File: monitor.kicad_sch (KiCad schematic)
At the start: 54 parts, among them J1 USB_C_Plug, J2 USB_C_Receptacle_USB2.0_14P, J3 Display, J4 Program, J5 Boot, U1 STM32U031K8Ux, U2 TPSM365R6V3RDNR, U3 TMP117xxDRV, U4 REF5025ADGK, U5 CC6903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

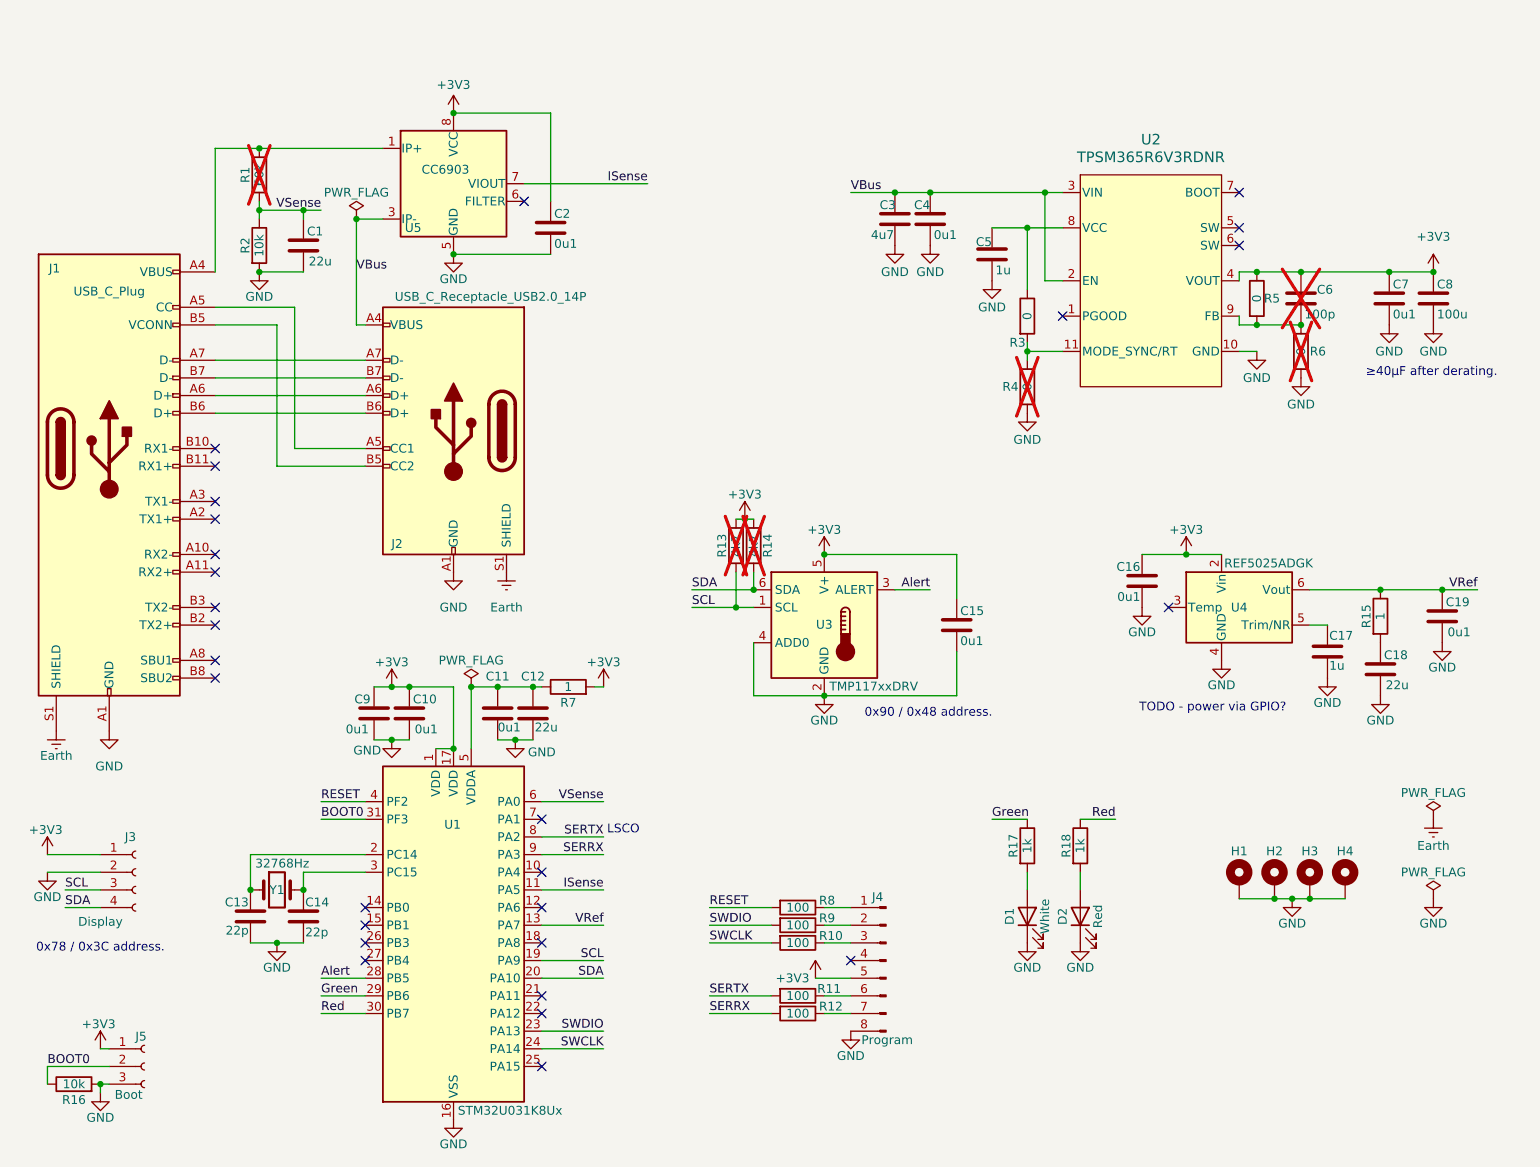
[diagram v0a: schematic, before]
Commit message: Monitor board layout
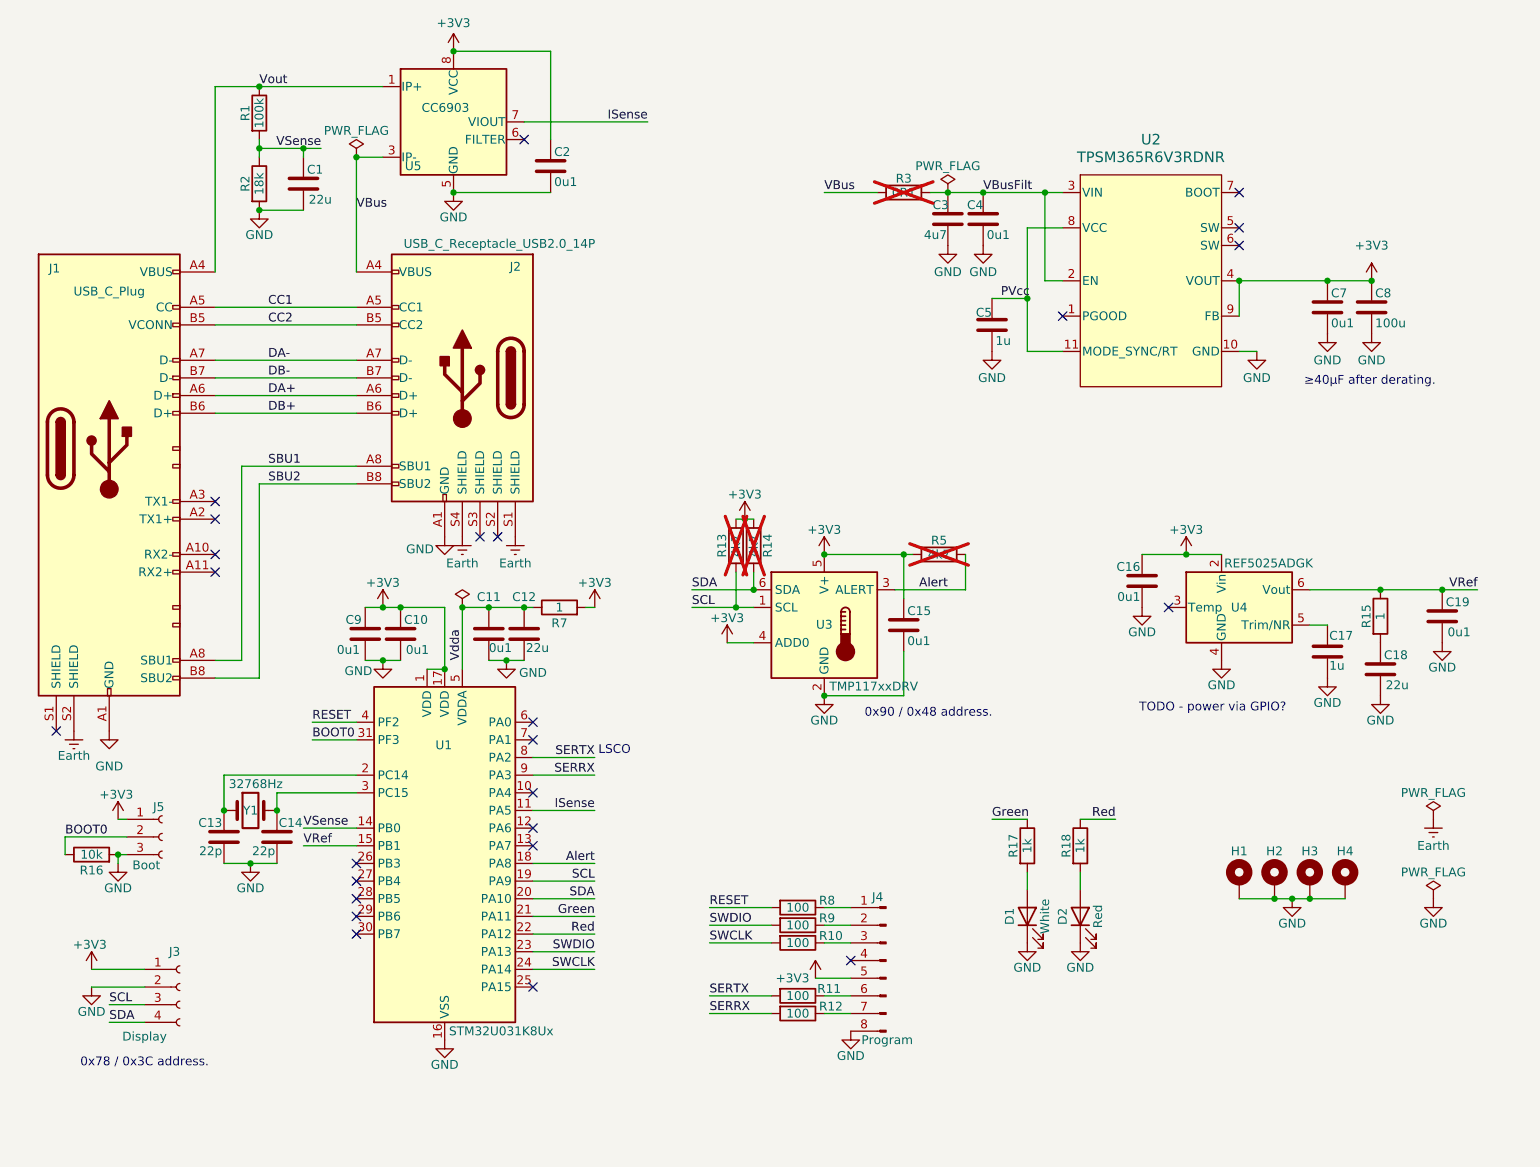
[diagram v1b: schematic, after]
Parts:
- removed C6: 100p, Capacitor_SMD:C_0603_1608Metric, symbol Device:C
- removed R4, R6: 0, Resistor_SMD:R_0603_1608Metric, symbol Device:R
- H1, H2, H3, H4: footprint MountingHole:MountingHole_3mm_Pad -> Parts:MountingHole_3mm_Pad
- J1: symbol Parts:USB_C_Plug -> Parts:USB_C_Plug_20; now in the parts list
- J2: footprint Connector_USB:USB_C_Receptacle_HRO_TYPE-C-31-M-12 -> Parts:USB_C_Receptacle_16P; symbol Parts:USB_C_Receptacle_USB2.0_14P -> Parts:USB_C_Receptacle_USB2.0_16P; now in the parts list
- J3: footprint Connector_PinSocket_2.54mm:PinSocket_1x03_P2.54mm_Vertical -> Parts:PinHeader_1x04_P2.54mm_Vertical
- J4: footprint Connector_PinHeader_2.54mm:PinHeader_1x08_P2.54mm_Vertical -> Parts:PinHeader_1x08_P2.54mm_Vertical
- J5: footprint Connector_PinSocket_2.54mm:PinSocket_1x03_P2.54mm_Vertical -> Parts:PinHeader_1x03_P2.54mm_Vertical
- R1: value 60k -> 100k; JLCPCB (none) -> C25803; now fitted
- R2: value 10k -> 18k; footprint Resistor_SMD:R_0402_1005Metric -> Resistor_SMD:R_0603_1608Metric; JLCPCB C25744 -> C25810
- R3: value 0 -> 0R1; JLCPCB C21189 -> (none); now not fitted; now left out of the parts list
- R5: value 0 -> 4k7; JLCPCB C21189 -> (none); now not fitted; now left out of the parts list
- U3: footprint Package_SON:WSON-6-1EP_2x2mm_P0.65mm_EP1x1.6mm -> Parts:WSON-6-1EP_2x2mm_P0.65mm_NoEP; symbol Sensor_Temperature:TMP117xxDRV -> Parts:TMP117xxDRV
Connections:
- net +3V3: now also U2.9 (FB), U3.4 (ADD0)
- net Alert: now also R5.2, U1.18 (PA8); no longer U1.28 (PB5)
- net Earth: now also J1.S2 (SHIELD), J2.S4 (SHIELD); no longer J1.S1 (SHIELD)
- net GND: no longer U3.4 (ADD0)
- net Green: now also U1.21 (PA11); no longer U1.29 (PB6)
- net Red: now also U1.22 (PA12); no longer U1.30 (PB7)
- net VBus: now also R3.1; no longer C3.1, C4.1, U2.2 (EN), U2.3 (VIN)
- net VRef: now also U1.15 (PB1); no longer U1.13 (PA7)
- net VSense: now also U1.14 (PB0); no longer U1.6 (PA0)
- net CC1: now reaches J1.A5 (CC), J2.A5 (CC1)
- net DA+: now reaches J1.A6 (D+), J2.A6 (D+)
- net DA-: now reaches J1.A7 (D-), J2.A7 (D-)
- net CC2: now reaches J1.B5 (VCONN), J2.B5 (CC2)
- net DB+: now reaches J1.B6 (D+), J2.B6 (D+)
- net DB-: now reaches J1.B7 (D-), J2.B7 (D-)
- net Vdda: now reaches C11.1, C12.1, R7.1, U1.5 (VDDA)
- net PVcc: now reaches U2.11 (MODE_SYNC/RT)
- net PVcc: now also C5.1, U2.8 (VCC); no longer R3.2
- net Vout: now reaches J1.A4 (VBUS), J1.A9 (VBUS), J1.B4 (VBUS), J1.B9 (VBUS), R1.1, U5.1 (IP+), U5.2 (IP+)
- net SBU1: now reaches J1.A8 (SBU1)
- net SBU1: now also J2.A8 (SBU1)
- net SBU2: now reaches J1.B8 (SBU2)
- net SBU2: now also J2.B8 (SBU2)
- new net VBusFilt: C3.1, C4.1, R3.2, U2.2 (EN), U2.3 (VIN)
- no-connect marks 28 -> 25
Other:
- moved on the sheet: C1, C10, C11, C12, C13, C14, C15, C2, C3, C4, C5, C7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

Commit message: Manufacturing updates
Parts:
- J1, J2: now left out of the parts list
- R1: now in the parts list
- U4: JLCPCB C75881 -> C75881
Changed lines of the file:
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@@
 		(unit 1)
 		(exclude_from_sim no)
-		(in_bom yes)
+		(in_bom no)
 		(on_board yes)
 		(dnp no)
@@
 			)
 		)
-		(property "JLCPCB" " C75881"
+		(property "JLCPCB" "C75881"
 			(at 201.93 102.87 0)
 			(effects
@@
 		(unit 1)
 		(exclude_from_sim no)
-		(in_bom no)
+		(in_bom yes)
 		(on_board yes)
 		(dnp no)
@@
 		(unit 1)
 		(exclude_from_sim no)
-		(in_bom yes)
+		(in_bom no)
 		(on_board yes)
 		(dnp no)

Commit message: Robustify reset
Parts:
- added C20: 0u1, Capacitor_SMD:C_0402_1005Metric, symbol Device:C
- added R19: 10k, Resistor_SMD:R_0603_1608Metric, symbol Device:R
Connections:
- net +3V3: now also R19.2
- net GND: now also C20.2
- net RESET: now also C20.1
- net at J4.1 (Pin_1), R8.1: now also R19.1

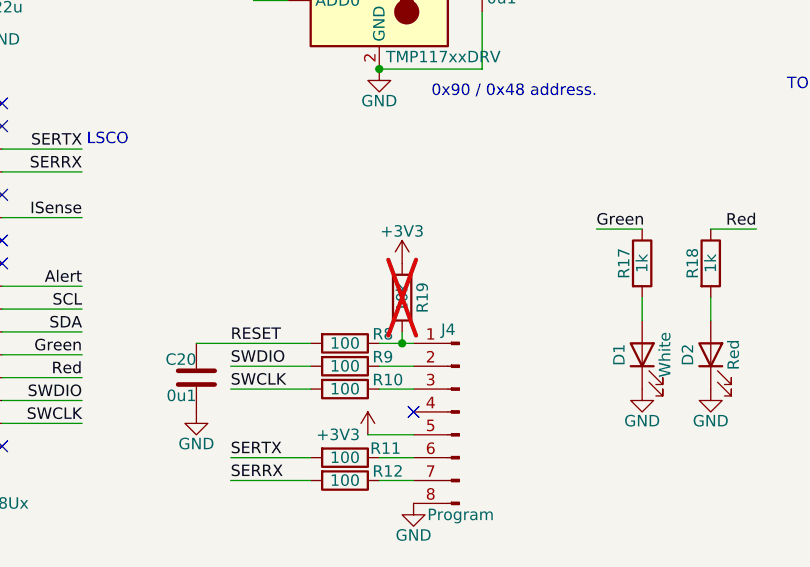
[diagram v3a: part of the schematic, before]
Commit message: Second board layout routed.
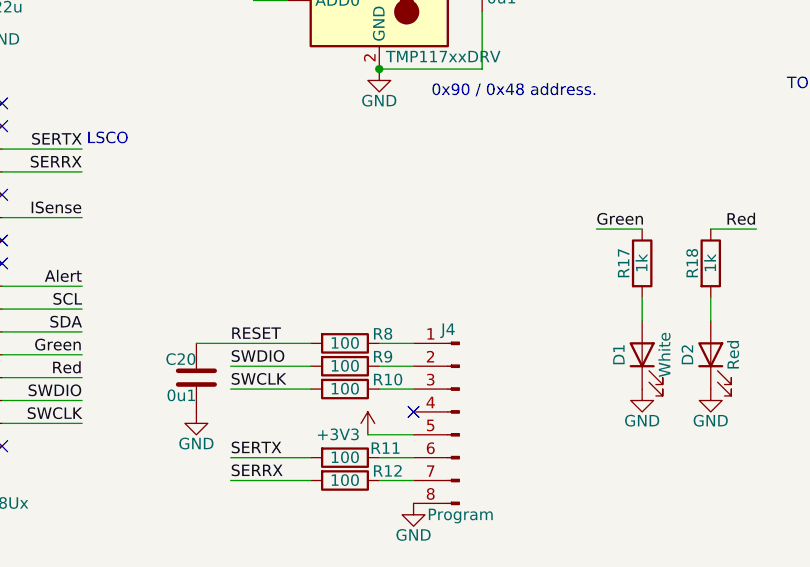
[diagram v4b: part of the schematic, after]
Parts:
- removed R19: 10k, Resistor_SMD:R_0603_1608Metric, symbol Device:R
- R7: footprint Resistor_SMD:R_0603_1608Metric -> Resistor_SMD:R_0402_1608Metric; JLCPCB C22936 -> C25086
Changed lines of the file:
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@@
 	)
 	(junction
-		(at 144.78 146.05)
-		(diameter 0)
-		(color 0 0 0 0)
-	)
-	(junction
 		(at 63.5 132.08)
 		(diameter 0)
@@
 	(wire
 		(pts
-			(xy 144.78 146.05) (xy 146.05 146.05)
-		)
-		(stroke
-			(width 0)
-			(type default)
-		)
-	)
-	(wire
-		(pts
 			(xy 222.25 100.33) (xy 231.14 100.33)
 		)
@@
 	(wire
 		(pts
-			(xy 142.24 146.05) (xy 144.78 146.05)
+			(xy 142.24 146.05) (xy 146.05 146.05)
 		)
 		(stroke
@@
 	(wire
 		(pts
-			(xy 144.78 144.78) (xy 144.78 146.05)
-		)
-		(stroke
-			(width 0)
-			(type default)
-		)
-	)
-	(wire
-		(pts
 			(xy 142.24 151.13) (xy 146.05 151.13)
 		)
@@
 	)
 	(symbol
-		(lib_id "power:+3V3")
-		(at 144.78 137.16 0)
-		(unit 1)
-		(exclude_from_sim no)
-		(in_bom yes)
-		(on_board yes)
-		(dnp no)
-		(property "Reference" "#PWR094"
-			(at 144.78 140.97 0)
-			(effects
-				(font
-					(size 1.27 1.27)
-				)
-				(hide yes)
-			)
-		)
-		(property "Value" "+3V3"
-			(at 144.78 133.604 0)
-			(effects
-				(font
-					(size 1.27 1.27)
-				)
-			)
-		)
-		(property "Footprint" ""
-			(at 144.78 137.16 0)
-			(effects
-				(font
-					(size 1.27 1.27)
-				)
-				(hide yes)
-			)
-		)
-		(property "Datasheet" ""
-			(at 144.78 137.16 0)
-			(effects
-				(font
-					(size 1.27 1.27)
-				)
-				(hide yes)
-			)
-		)
-		(property "Description" "Power symbol creates a global label with name \"+3V3\""
-			(at 144.78 137.16 0)
-			(effects
-				(font
-					(size 1.27 1.27)
-				)
-				(hide yes)
-			)
-		)
-		(pin "1"
-		)
-		(instances
-			(project "monitor"
-				(path "/86951f79-24f8-43b4-b1f7-cdfc83343ec0"
-					(reference "#PWR094")
-					(unit 1)
-				)
-			)
-		)
-	)
-	(symbol
 		(lib_id "Device:C")
 		(at 214.63 109.22 0)
@@
 			)
 		)
-		(property "Footprint" "Resistor_SMD:R_0603_1608Metric"
+		(property "Footprint" "Resistor_SMD:R_0402_1608Metric"
 			(at 104.14 104.648 90)
 			(effects
@@
 			)
 		)
-		(property "JLCPCB" "C22936"
+		(property "JLCPCB" "C25086"
 			(at 104.14 102.87 0)
 			(effects
@@
 					(unit 1)
 				)
-			)
-		)
-	)
-	(symbol
-		(lib_id "Device:R")
-		(at 144.78 140.97 180)
-		(unit 1)
-		(exclude_from_sim no)
-		(in_bom no)
-		(on_board yes)
-		(dnp yes)
-		(property "Reference" "R19"
-			(at 146.304 140.9701 90)
-			(do_not_autoplace yes)
-			(effects
-				(font
-					(size 1.27 1.27)
-				)
-				(justify bottom)
-			)
-		)
-		(property "Value" "10k"
-			(at 144.78 140.9701 90)
-			(effects
-				(font
-					(size 1.27 1.27)
-				)
-			)
-		)
-		(property "Footprint" "Resistor_SMD:R_0603_1608Metric"
-			(at 146.558 140.97 90)
-			(effects
-				(font
-					(size 1.27 1.27)
-				)
-				(hide yes)
-			)
-		)
-		(property "Datasheet" "~"
-			(at 144.78 140.97 0)
-			(effects
-				(font
-					(size 1.27 1.27)
-				)
-				(hide yes)
-			)
-		)
-		(property "Description" "Resistor"
-			(at 144.78 140.97 0)
-			(effects
-				(font
-					(size 1.27 1.27)
-				)
-				(hide yes)
-			)
-		)
-		(property "JLCPCB" ""
-			(at 144.78 140.97 0)
-			(effects
-				(font
-					(size 1.27 1.27)
-				)
-				(hide yes)
-			)
-		)
-		(pin "2"
-		)
-		(pin "1"
-		)
-		(instances
-			(project "monitor"
-				(path "/86951f79-24f8-43b4-b1f7-cdfc83343ec0"
-					(reference "R19")
-					(unit 1)
-				)
